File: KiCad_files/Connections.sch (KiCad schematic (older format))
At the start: 4 parts, among them U1 XC7A35T_CSG325

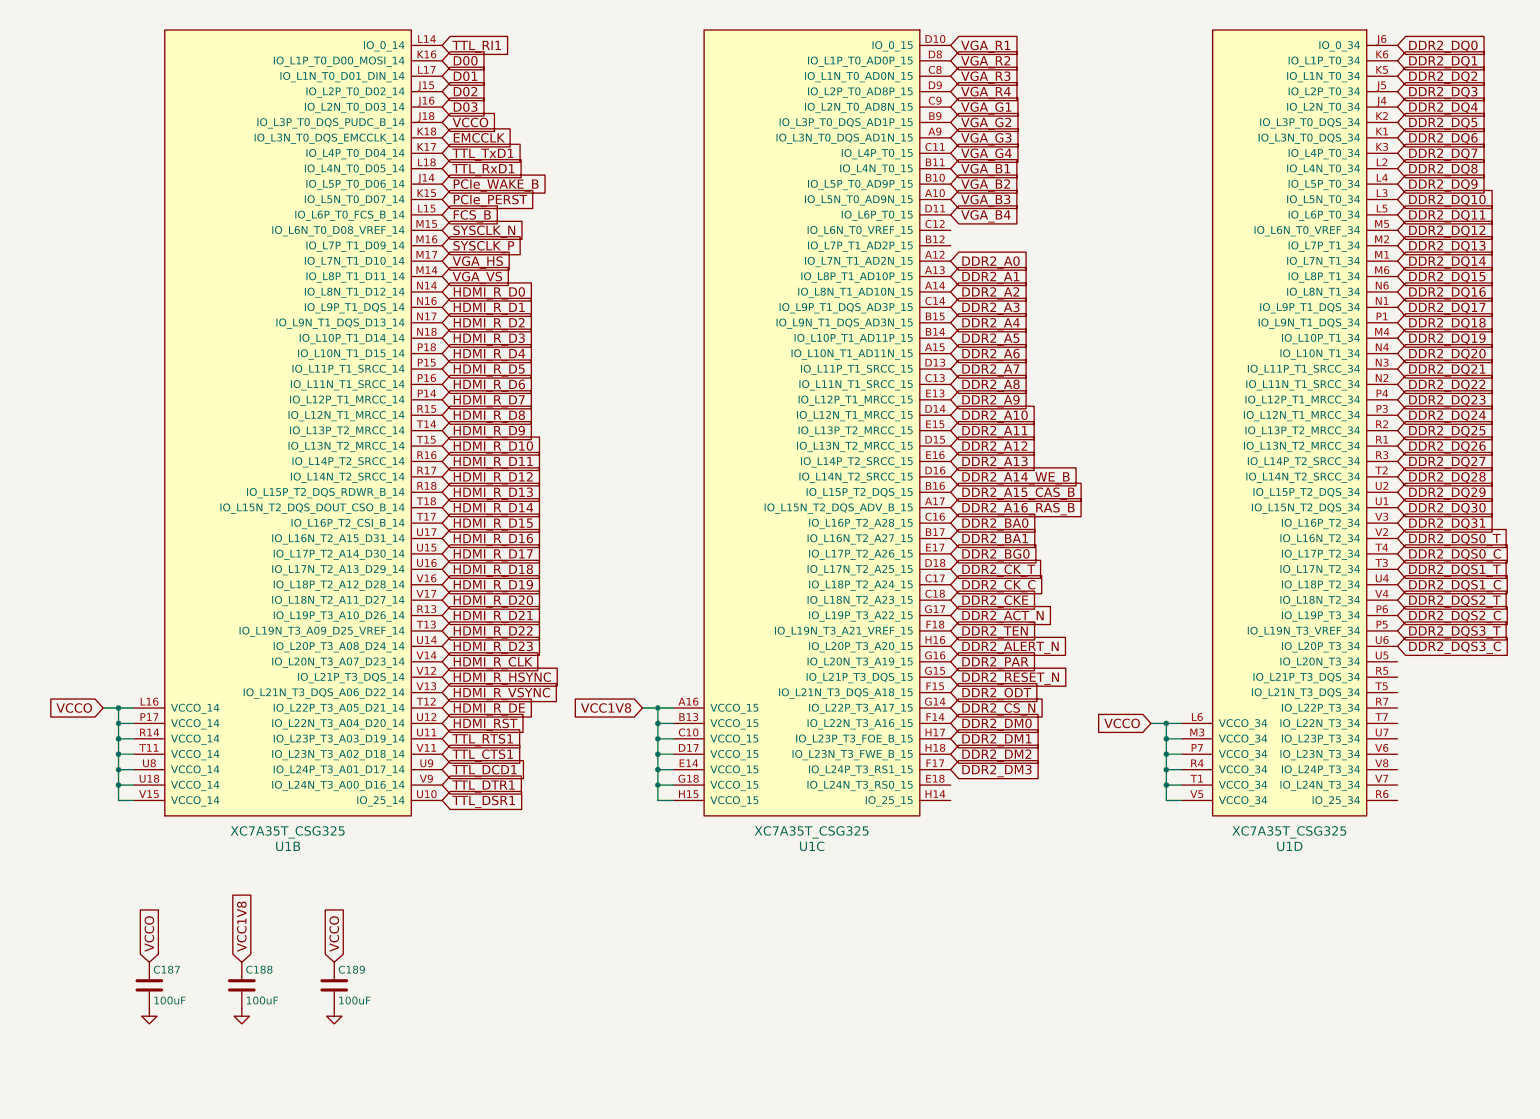
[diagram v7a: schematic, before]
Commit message: Cleanup for DRC and HDMI. HDMI and DDR2 looks good
DRC returns 5 errors with POWEROUTPUT-POWEROUTPUT set as good.
3 of them come from 3V3 since it's being driven from a MOSFET.
1 of them from VCC5V0 not yet supplied.
1 of them from USB_VBUS not set as output.
TODO:
5V supply for HDMI
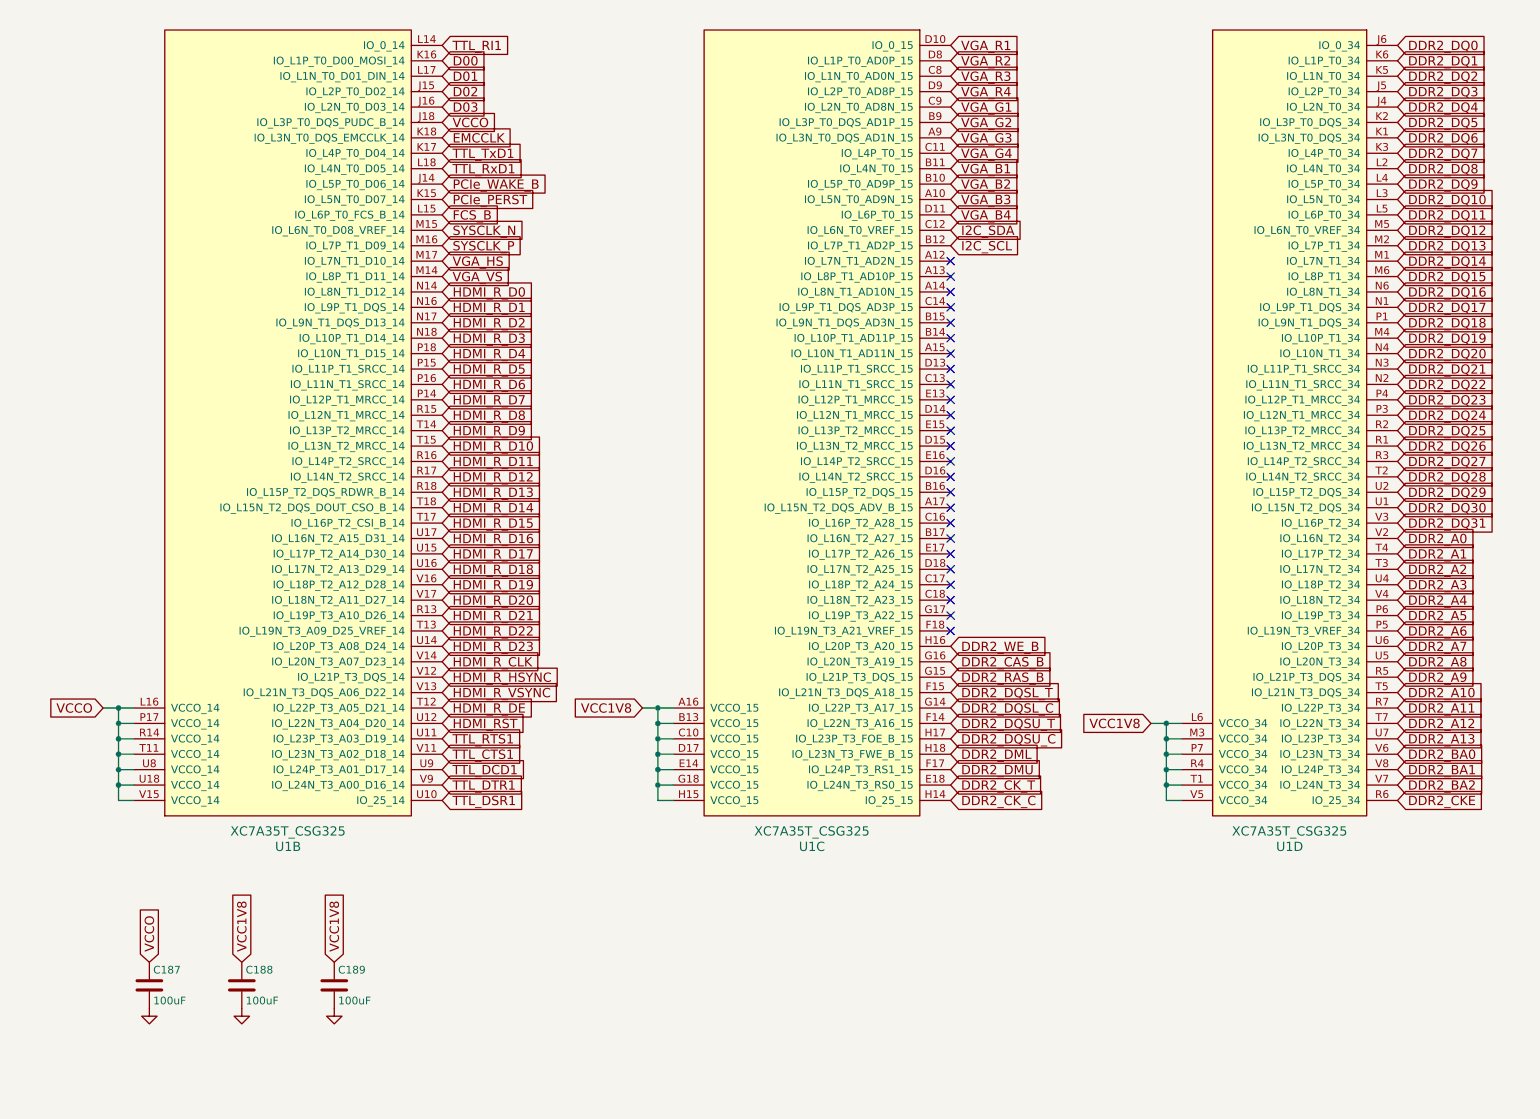
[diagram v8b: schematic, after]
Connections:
- net DDR2_DQS0_C is gone; now on net DDR2_A1: U1.T4 (IO_L17P_T2_34)
- net DDR2_DQS0_T is gone; now on net DDR2_A0: U1.V2 (IO_L16N_T2_34)
- net DDR2_DQS1_C is gone; now on net DDR2_A3: U1.U4 (IO_L18P_T2_34)
- net DDR2_DQS1_T is gone; now on net DDR2_A2: U1.T3 (IO_L17N_T2_34)
- net DDR2_DQS2_C is gone; now on net DDR2_A5: U1.P6 (IO_L19P_T3_34)
- net DDR2_DQS2_T is gone; now on net DDR2_A4: U1.V4 (IO_L18N_T2_34)
- net DDR2_DQS3_C is gone; now on net DDR2_A7: U1.U6 (IO_L20P_T3_34)
- net DDR2_DQS3_T is gone; now on net DDR2_A6: U1.P5 (IO_L19N_T3_VREF_34)
- net DDR2_A0: no longer U1.A12 (IO_L7N_T1_AD2N_15)
- net DDR2_A1: no longer U1.A13 (IO_L8P_T1_AD10P_15)
- net DDR2_A10: now also U1.T5 (IO_L21N_T3_DQS_34); no longer U1.D14 (IO_L12N_T1_MRCC_15)
- net DDR2_A11: now also U1.R7 (IO_L22P_T3_34); no longer U1.E15 (IO_L13P_T2_MRCC_15)
- net DDR2_A12: now also U1.T7 (IO_L22N_T3_34); no longer U1.D15 (IO_L13N_T2_MRCC_15)
- net DDR2_A13: now also U1.U7 (IO_L23P_T3_34); no longer U1.E16 (IO_L14P_T2_SRCC_15)
- net DDR2_A2: no longer U1.A14 (IO_L8N_T1_AD10N_15)
- net DDR2_A3: no longer U1.C14 (IO_L9P_T1_DQS_AD3P_15)
- net DDR2_A4: no longer U1.B15 (IO_L9N_T1_DQS_AD3N_15)
- net DDR2_A5: no longer U1.B14 (IO_L10P_T1_AD11P_15)
- net DDR2_A6: no longer U1.A15 (IO_L10N_T1_AD11N_15)
- net DDR2_A7: no longer U1.D13 (IO_L11P_T1_SRCC_15)
- net DDR2_A8: now also U1.U5 (IO_L20N_T3_34); no longer U1.C13 (IO_L11N_T1_SRCC_15)
- net DDR2_A9: now also U1.R5 (IO_L21P_T3_DQS_34); no longer U1.E13 (IO_L12P_T1_MRCC_15)
- net DDR2_BA0: now also U1.V6 (IO_L23N_T3_34); no longer U1.C16 (IO_L16P_T2_A28_15)
- net DDR2_BA1: now also U1.V8 (IO_L24P_T3_34); no longer U1.B17 (IO_L16N_T2_A27_15)
- net DDR2_CKE: now also U1.R6 (IO_25_34); no longer U1.C18 (IO_L18N_T2_A23_15)
- net DDR2_CK_C: now also U1.H14 (IO_25_15); no longer U1.C17 (IO_L18P_T2_A24_15)
- net DDR2_CK_T: now also U1.E18 (IO_L24N_T3_RS0_15); no longer U1.D18 (IO_L17N_T2_A25_15)
- net VCC1V8: now also C189.1, U1.L6 (VCCO_34), U1.M3 (VCCO_34), U1.P7 (VCCO_34), U1.R4 (VCCO_34), U1.T1 (VCCO_34), U1.V5 (VCCO_34)
- net VCCO: no longer C189.1, U1.L6 (VCCO_34), U1.M3 (VCCO_34), U1.P7 (VCCO_34), U1.R4 (VCCO_34), U1.T1 (VCCO_34), U1.V5 (VCCO_34)
- net I2C_SCL: now reaches U1.B12 (IO_L7P_T1_AD2P_15)
- net I2C_SDA: now reaches U1.C12 (IO_L6N_T0_VREF_15)
- net DDR2_BA2: now reaches U1.V7 (IO_L24N_T3_34)
- net DDR2_A14_WE_B: no longer names the net of U1.D16 (IO_L14N_T2_SRCC_15)
- net DDR2_A15_CAS_B: no longer names the net of U1.B16 (IO_L15P_T2_DQS_15)
- net DDR2_A16_RAS_B: no longer names the net of U1.A17 (IO_L15N_T2_DQS_ADV_B_15)
- net DDR2_ACT_N: no longer names the net of U1.G17 (IO_L19P_T3_A22_15)
- net DDR2_ALERT_N renamed DDR2_WE_B
- net DDR2_BG0: no longer names the net of U1.E17 (IO_L17P_T2_A26_15)
- net DDR2_CS_N renamed DDR2_DQSL_C
- net DDR2_DM0 renamed DDR2_DQSU_T
- net DDR2_DM1 renamed DDR2_DQSU_C
- net DDR2_DM2 renamed DDR2_DML
- net DDR2_DM3 renamed DDR2_DMU
- net DDR2_ODT renamed DDR2_DQSL_T
- net DDR2_PAR renamed DDR2_CAS_B
- net DDR2_RESET_N renamed DDR2_RAS_B
- net DDR2_TEN: no longer names the net of U1.F18 (IO_L19N_T3_A21_VREF_15)
- no-connect marks 0 -> 25
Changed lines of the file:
@@
 $EndComp
 Text GLabel 7800 5500 0    60   Input ~ 0
-VCCO
+VCC1V8
 Wire Wire Line
 	7800 5500 7900 5500
@@
 $EndComp
 Text GLabel 2500 7050 1    60   Input ~ 0
-VCCO
+VCC1V8
 $Comp
 L power:GND #PWR099
@@
 U 2 1 5C174C53
 P 2200 6000
+AR Path="/5C174C53" Ref="U1"  Part="2"
+AR Path="/5C064F83/5C174C53" Ref="U1"  Part="2"
 F 0 "U1" H 2200 5700 60  0000 C CNN
 F 1 "XC7A35T_CSG325" H 2200 5800 60  0000 C CNN
@@
 U 3 1 5C174C9A
 P 5600 6000
+AR Path="/5C174C9A" Ref="U1"  Part="3"
+AR Path="/5C064F83/5C174C9A" Ref="U1"  Part="3"
 F 0 "U1" H 5600 5700 60  0000 C CNN
 F 1 "XC7A35T_CSG325" H 5600 5800 60  0000 C CNN
@@
 U 4 1 5C174CD5
 P 8700 6000
+AR Path="/5C174CD5" Ref="U1"  Part="4"
+AR Path="/5C064F83/5C174CD5" Ref="U1"  Part="4"
 F 0 "U1" H 8700 5700 60  0000 C CNN
 F 1 "XC7A35T_CSG325" H 8700 5800 60  0000 C CNN
@@
 Text GLabel 3200 2600 2    60   Input ~ 0
 VGA_VS
-Text GLabel 6500 2500 2    60   Input ~ 0
+Text GLabel 9400 4300 2    60   Input ~ 0
 DDR2_A0
-Text GLabel 6500 2600 2    60   Input ~ 0
+Text GLabel 9400 4400 2    60   Input ~ 0
 DDR2_A1
-Text GLabel 6500 2700 2    60   Input ~ 0
+Text GLabel 9400 4500 2    60   Input ~ 0
 DDR2_A2
-Text GLabel 6500 2800 2    60   Input ~ 0
+Text GLabel 9400 4600 2    60   Input ~ 0
 DDR2_A3
-Text GLabel 6500 2900 2    60   Input ~ 0
+Text GLabel 9400 4700 2    60   Input ~ 0
 DDR2_A4
-Text GLabel 6500 3000 2    60   Input ~ 0
+Text GLabel 9400 4800 2    60   Input ~ 0
 DDR2_A5
-Text GLabel 6500 3100 2    60   Input ~ 0
+Text GLabel 9400 4900 2    60   Input ~ 0
 DDR2_A6
-Text GLabel 6500 3200 2    60   Input ~ 0
+Text GLabel 9400 5000 2    60   Input ~ 0
 DDR2_A7
-Text GLabel 6500 3300 2    60   Input ~ 0
+Text GLabel 9400 5100 2    60   Input ~ 0
 DDR2_A8
-Text GLabel 6500 3400 2    60   Input ~ 0
+Text GLabel 9400 5200 2    60   Input ~ 0
 DDR2_A9
-Text GLabel 6500 3500 2    60   Input ~ 0
+Text GLabel 9400 5300 2    60   Input ~ 0
 DDR2_A10
-Text GLabel 6500 3600 2    60   Input ~ 0
+Text GLabel 9400 5400 2    60   Input ~ 0
 DDR2_A11
-Text GLabel 6500 3700 2    60   Input ~ 0
+Text GLabel 9400 5500 2    60   Input ~ 0
 DDR2_A12
-Text GLabel 6500 3800 2    60   Input ~ 0
+Text GLabel 9400 5600 2    60   Input ~ 0
 DDR2_A13
-Text GLabel 6500 3900 2    60   Input ~ 0
-DDR2_A14_WE_B
-Text GLabel 6500 4000 2    60   Input ~ 0
-DDR2_A15_CAS_B
-Text GLabel 6500 4100 2    60   Input ~ 0
-DDR2_A16_RAS_B
-Text GLabel 6500 4200 2    60   Input ~ 0
+Text GLabel 6500 5000 2    60   Input ~ 0
+DDR2_WE_B
+Text GLabel 6500 5100 2    60   Input ~ 0
+DDR2_CAS_B
+Text GLabel 6500 5200 2    60   Input ~ 0
+DDR2_RAS_B
+Text GLabel 9400 5700 2    60   Input ~ 0
 DDR2_BA0
-Text GLabel 6500 4300 2    60   Input ~ 0
+Text GLabel 9400 5800 2    60   Input ~ 0
 DDR2_BA1
-Text GLabel 6500 4400 2    60   Input ~ 0
-DDR2_BG0
-Text GLabel 6500 4500 2    60   Input ~ 0
+Text GLabel 9400 5900 2    60   Input ~ 0
+DDR2_BA2
+Text GLabel 6500 5900 2    60   Input ~ 0
 DDR2_CK_T
-Text GLabel 6500 4600 2    60   Input ~ 0
+Text GLabel 6500 6000 2    60   Input ~ 0
 DDR2_CK_C
-Text GLabel 6500 4700 2    60   Input ~ 0
+Text GLabel 9400 6000 2    60   Input ~ 0
 DDR2_CKE
-Text GLabel 6500 4800 2    60   Input ~ 0
-DDR2_ACT_N
-Text GLabel 6500 4900 2    60   Input ~ 0
-DDR2_TEN
-Text GLabel 6500 5000 2    60   Input ~ 0
-DDR2_ALERT_N
-Text GLabel 6500 5100 2    60   Input ~ 0
-DDR2_PAR
-Text GLabel 6500 5200 2    60   Input ~ 0
-DDR2_RESET_N
-Text GLabel 6500 5300 2    60   Input ~ 0
-DDR2_ODT
-Text GLabel 6500 5400 2    60   Input ~ 0
-DDR2_CS_N
 Text GLabel 9400 1100 2    60   Input ~ 0
 DDR2_DQ0
@@
 Text GLabel 9400 2600 2    60   Input ~ 0
 DDR2_DQ15
-Text GLabel 9400 4300 2    60   Input ~ 0
-DDR2_DQS0_T
-Text GLabel 9400 4400 2    60   Input ~ 0
-DDR2_DQS0_C
-Text GLabel 9400 4500 2    60   Input ~ 0
-DDR2_DQS1_T
-Text GLabel 9400 4600 2    60   Input ~ 0
-DDR2_DQS1_C
-Text GLabel 6500 5500 2    60   Input ~ 0
-DDR2_DM0
-Text GLabel 6500 5600 2    60   Input ~ 0
-DDR2_DM1
 Text GLabel 9400 2700 2    60   Input ~ 0
 DDR2_DQ16
@@
 Text GLabel 9400 4200 2    60   Input ~ 0
 DDR2_DQ31
-Text GLabel 9400 4700 2    60   Input ~ 0
-DDR2_DQS2_T
-Text GLabel 9400 4800 2    60   Input ~ 0
-DDR2_DQS2_C
-Text GLabel 9400 4900 2    60   Input ~ 0
-DDR2_DQS3_T
-Text GLabel 9400 5000 2    60   Input ~ 0
-DDR2_DQS3_C
+Wire Wire Line
+	1100 5400 1200 5400
+Wire Wire Line
+	1100 5900 1100 6000
+Wire Wire Line
+	1100 5800 1100 5900
+Wire Wire Line
+	1100 5700 1100 5800
+Wire Wire Line
+	1100 5600 1100 5700
+Wire Wire Line
+	1100 5500 1100 5600
+Wire Wire Line
+	4600 5400 4700 5400
+Wire Wire Line
+	4600 5900 4600 6000
+Wire Wire Line
+	4600 5800 4600 5900
+Wire Wire Line
+	4600 5700 4600 5800
+Wire Wire Line
+	4600 5600 4600 5700
+Wire Wire Line
+	4600 5500 4600 5600
+Wire Wire Line
+	7900 5500 8000 5500
+Wire Wire Line
+	7900 5900 7900 6000
+Wire Wire Line
+	7900 5800 7900 5900
+Wire Wire Line
+	7900 5700 7900 5800
+Wire Wire Line
+	7900 5600 7900 5700
+Text GLabel 6500 5300 2    60   Input ~ 0
+DDR2_DQSL_T
+Text GLabel 6500 5400 2    60   Input ~ 0
+DDR2_DQSL_C
+Text GLabel 6500 5500 2    60   Input ~ 0
+DDR2_DQSU_T
+Text GLabel 6500 5600 2    60   Input ~ 0
+DDR2_DQSU_C
+Text GLabel 6500 5800 2    60   Input ~ 0
+DDR2_DMU
 Text GLabel 6500 5700 2    60   Input ~ 0
-DDR2_DM2
-Text GLabel 6500 5800 2    60   Input ~ 0
-DDR2_DM3
-Wire Wire Line
-	1100 5400 1200 5400
-Wire Wire Line
-	1100 5900 1100 6000
-Wire Wire Line
-	1100 5800 1100 5900
-Wire Wire Line
-	1100 5700 1100 5800
-Wire Wire Line
-	1100 5600 1100 5700
-Wire Wire Line
-	1100 5500 1100 5600
-Wire Wire Line
-	4600 5400 4700 5400
-Wire Wire Line
-	4600 5900 4600 6000
-Wire Wire Line
-	4600 5800 4600 5900
-Wire Wire Line
-	4600 5700 4600 5800
-Wire Wire Line
-	4600 5600 4600 5700
-Wire Wire Line
-	4600 5500 4600 5600
-Wire Wire Line
-	7900 5500 8000 5500
-Wire Wire Line
-	7900 5900 7900 6000
-Wire Wire Line
-	7900 5800 7900 5900
-Wire Wire Line
-	7900 5700 7900 5800
-Wire Wire Line
-	7900 5600 7900 5700
+DDR2_DML
+NoConn ~ 6500 2500
+NoConn ~ 6500 2600
+NoConn ~ 6500 2700
+NoConn ~ 6500 2800
+NoConn ~ 6500 2900
+NoConn ~ 6500 3000
+NoConn ~ 6500 3100
+NoConn ~ 6500 3200
+NoConn ~ 6500 3300
+NoConn ~ 6500 3400
+NoConn ~ 6500 3500
+NoConn ~ 6500 3600
+NoConn ~ 6500 3700
+NoConn ~ 6500 3800
+NoConn ~ 6500 3900
+NoConn ~ 6500 4000
+NoConn ~ 6500 4100
+NoConn ~ 6500 4200
+NoConn ~ 6500 4300
+NoConn ~ 6500 4400
+NoConn ~ 6500 4500
+NoConn ~ 6500 4600
+NoConn ~ 6500 4700
+NoConn ~ 6500 4800
+NoConn ~ 6500 4900
+Text GLabel 6500 2400 2    60   Input ~ 0
+I2C_SCL
+Text GLabel 6500 2300 2    60   Input ~ 0
+I2C_SDA
 $EndSCHEMATC
